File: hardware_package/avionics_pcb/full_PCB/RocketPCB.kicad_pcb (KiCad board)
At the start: 2 copper layers, 74 parts, among them J1 USB_C_Receptacle, J2 Micro_SD_Card, J3 Conn_01x03_Female, Q1 DMG2301L, Q2 Q_PMOS_DGS, SW1 SW_Push, SW2 SW_Push, U1 STM32F405RGTx, U2 TPS62160DSG, U3 Radio_Header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

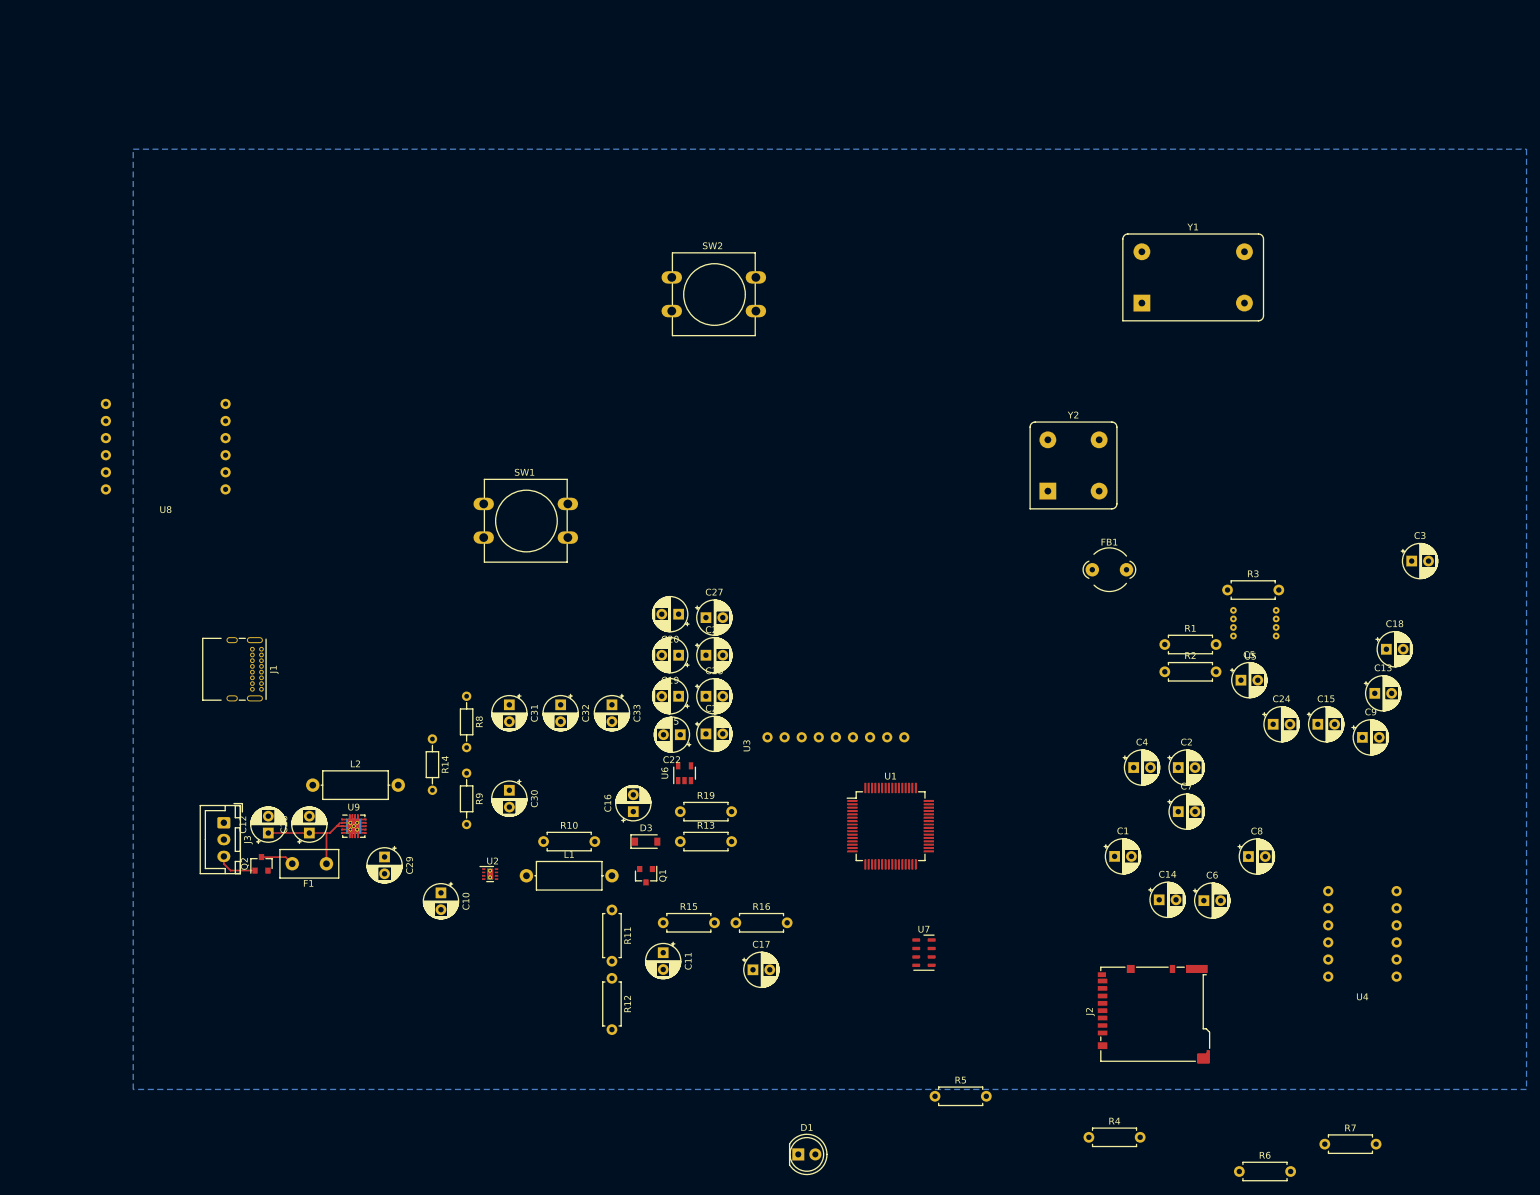
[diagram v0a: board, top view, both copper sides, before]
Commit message: Added test points and LEDs for debug, also added decoupling capacitors
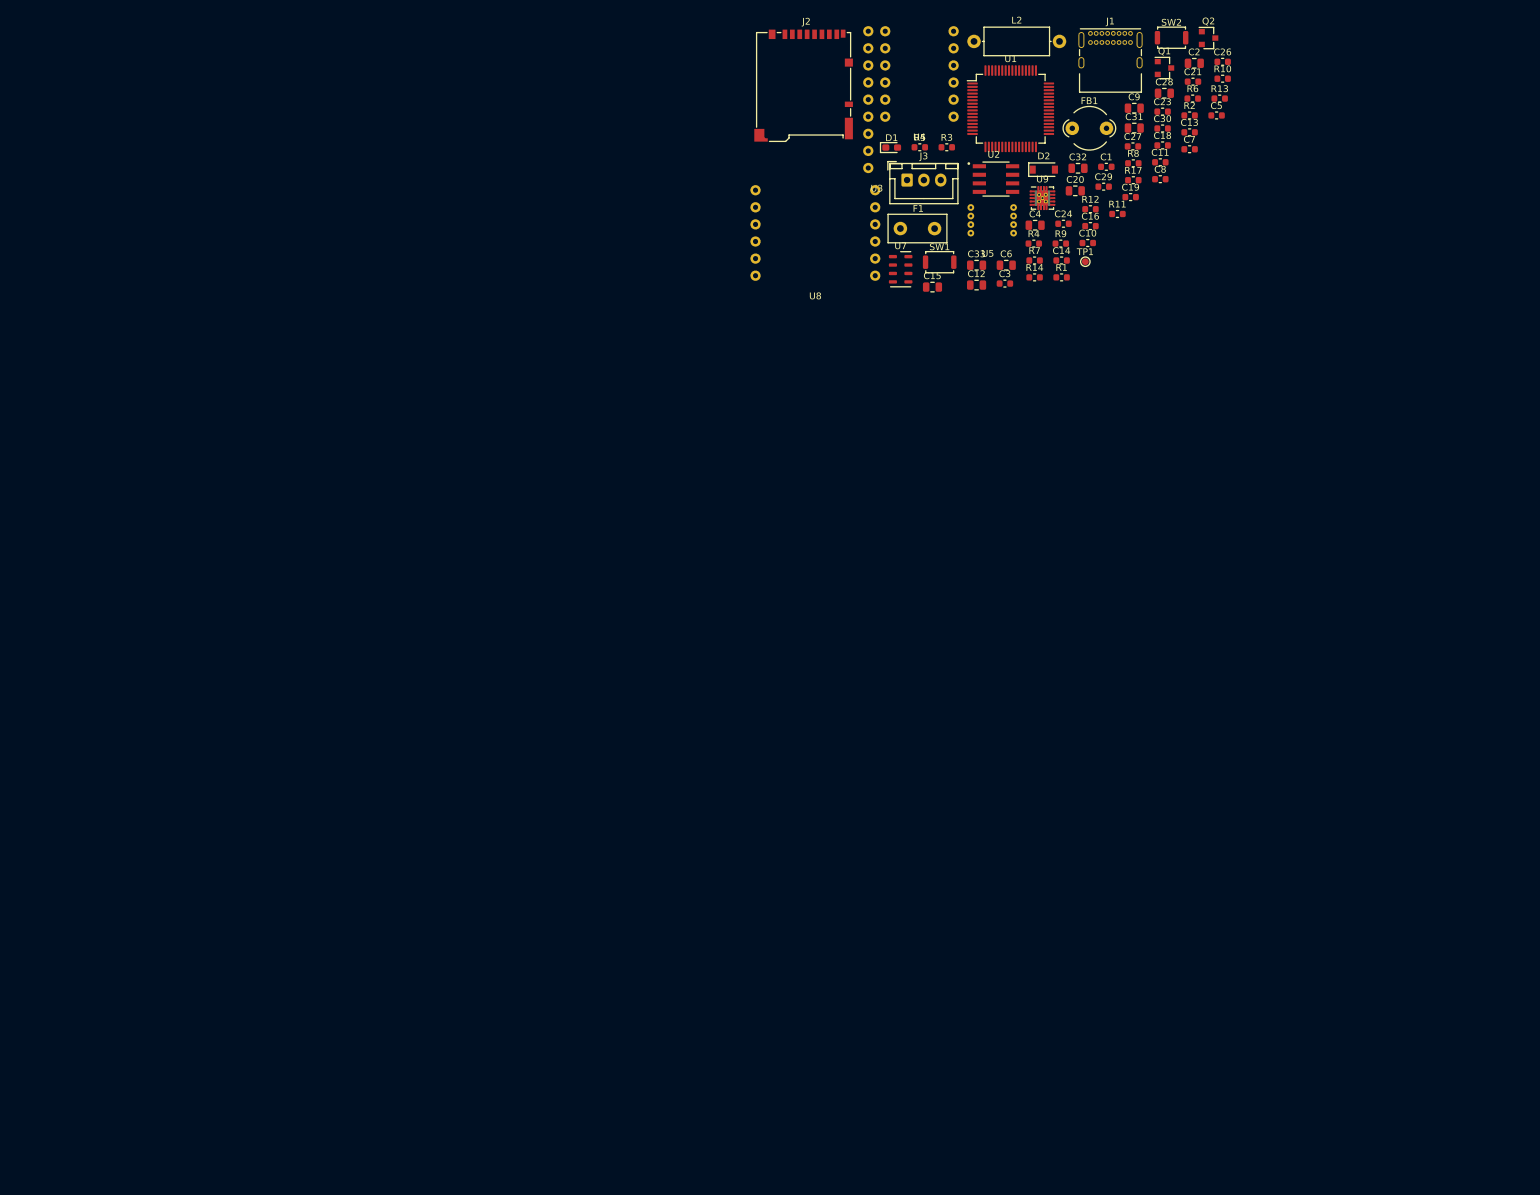
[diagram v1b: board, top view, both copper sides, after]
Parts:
- removed C17, C25: 1uF, Capacitor_THT:CP_Radial_D5.0mm_P2.50mm
- removed C22: 10uF, Capacitor_THT:CP_Radial_D5.0mm_P2.50mm
- removed D3: MBR0540, Diode_SMD:D_SOD-123
- removed L1: 2.2uH, Inductor_THT:L_Axial_L9.5mm_D4.0mm_P12.70mm_Horizontal_Fastron_SMCC
- removed R15, R16: 100k, Resistor_THT:R_Axial_DIN0207_L6.3mm_D2.5mm_P7.62mm_Horizontal
- removed R19: 10k, Resistor_THT:R_Axial_DIN0207_L6.3mm_D2.5mm_P7.62mm_Horizontal
- removed U6: AP2112K-3.3, Package_TO_SOT_SMD:SOT-23-5
- removed Y1: 12MHz, Oscillator:Oscillator_DIP-14_LargePads
- removed Y2: 32MHz, Oscillator:Oscillator_DIP-8_LargePads
- added D2: MBR0540, Diode_SMD:D_SOD-123, F.Cu at (215.3, 13.2)
- added R17: 4.7k, Resistor_SMD:R_0603_1608Metric, F.Cu at (228.6, 14.8)
- added TP1: TestPoint, TestPoint:TestPoint_Pad_D1.0mm, F.Cu at (221.5, 26.9)
- C1, C3: value 22pF -> 1uF; footprint Capacitor_THT:CP_Radial_D5.0mm_P2.50mm -> Capacitor_SMD:C_0603_1608Metric
- C10, C16: value 10uF -> 0.1uF; footprint Capacitor_THT:CP_Radial_D5.0mm_P2.50mm -> Capacitor_SMD:C_0603_1608Metric
- C11: value 22uF -> 0.1uF; footprint Capacitor_THT:CP_Radial_D5.0mm_P2.50mm -> Capacitor_SMD:C_0603_1608Metric
- C12, C15, C20, C28, C31, C32, C33, C4, C6, C9: footprint Capacitor_THT:CP_Radial_D5.0mm_P2.50mm -> Capacitor_SMD:C_0805_2012Metric
- C13: value 0.1u -> 0.1uF; footprint Capacitor_THT:CP_Radial_D5.0mm_P2.50mm -> Capacitor_SMD:C_0603_1608Metric
- C14: value 2.2u -> 2.2uF; footprint Capacitor_THT:CP_Radial_D5.0mm_P2.50mm -> Capacitor_SMD:C_0603_1608Metric
- C18, C19, C21, C23, C24, C26, C27, C29, C30, C5, C8: footprint Capacitor_THT:CP_Radial_D5.0mm_P2.50mm -> Capacitor_SMD:C_0603_1608Metric
- C2: value 22pF -> 10uF; footprint Capacitor_THT:CP_Radial_D5.0mm_P2.50mm -> Capacitor_SMD:C_0805_2012Metric
- C7: value 22pF -> C; footprint Capacitor_THT:CP_Radial_D5.0mm_P2.50mm -> Capacitor_SMD:C_0603_1608Metric
- D1: footprint LED_THT:LED_D5.0mm_Clear -> LED_SMD:LED_0603_1608Metric_Pad1.05x0.95mm_HandSolder
- Q2: value Q_PMOS_DGS -> DMG2301L
- R1, R2, R3, R4, R5, R6, R7: footprint Resistor_THT:R_Axial_DIN0207_L6.3mm_D2.5mm_P7.62mm_Horizontal -> Resistor_SMD:R_0603_1608Metric
- R10: value 100k -> 10k; footprint Resistor_THT:R_Axial_DIN0207_L6.3mm_D2.5mm_P7.62mm_Horizontal -> Resistor_SMD:R_0603_1608Metric
- R11: value 649k -> 100k; footprint Resistor_THT:R_Axial_DIN0207_L6.3mm_D2.5mm_P7.62mm_Horizontal -> Resistor_SMD:R_0603_1608Metric
- R12: value 180k -> 4.7K; footprint Resistor_THT:R_Axial_DIN0207_L6.3mm_D2.5mm_P7.62mm_Horizontal -> Resistor_SMD:R_0603_1608Metric
- R13: value 100k -> 4.7k; footprint Resistor_THT:R_Axial_DIN0207_L6.3mm_D2.5mm_P7.62mm_Horizontal -> Resistor_SMD:R_0603_1608Metric
- R14, R8, R9: footprint Resistor_THT:R_Axial_DIN0204_L3.6mm_D1.6mm_P7.62mm_Horizontal -> Resistor_SMD:R_0603_1608Metric
- SW1, SW2: footprint Button_Switch_THT:SW_PUSH-12mm -> Button_Switch_SMD:SW_Push_SPST_NO_Alps_SKRK
- U2: value TPS62160DSG -> UCC381DP-3; footprint Package_SON:WSON-8-1EP_2x2mm_P0.5mm_EP0.9x1.6mm_ThermalVias -> 3v3 _linReg:SOIC127P599X175-8N
- moved Q2 186.7 mm to (239.8, -6.35), turned to 0 degrees
- moved C28 168.0 mm to (233.2, 1.85), turned to 0 degrees
- moved R6 159.6 mm to (237.4, 2.64)
- moved J1 153.4 mm to (222.2, -7.04), turned to 0 degrees
- moved R10 151.7 mm to (241.9, -0.31)
- moved D1 150.2 mm to (192.7, 9.92)
- moved L2 147.9 mm to (204.9, -5.85)
- moved J2 147.5 mm to (179.6, 0.72), turned to 0 degrees
- moved C29 146.1 mm to (224.2, 15.7), turned to 0 degrees
- moved U4 143.7 mm to (196.8, 7.87)
- moved Q1 142.6 mm to (233.2, -1.90), turned to 0 degrees
- moved R5 141.0 mm to (196.9, 9.88)
- moved J3 139.4 mm to (195.0, 14.7), turned to 0 degrees
- moved C11 138.7 mm to (232.6, 12.1), turned to 0 degrees
- moved U9 138.5 mm to (215.1, 17.4)
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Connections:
- net /~RESET~ renamed ~RESET~
- C1 pad 1: Net-(C1-Pad1) -> +3V3
- C10 pad 1: +7.5V -> GND
- C10 pad 2: GND -> +3V3
- C11 pad 1: +BATT -> +3V3
- C12 pad 1: +7.5V -> +7V4
- C16 pad 1: Net-(C16-Pad1) -> +3V3
- C2 pad 1: Net-(C2-Pad1) -> GND
- C2 pad 2: GND -> +3V3
- C28 pad 1: +7.5V -> +7V4
- C7 pad 1: Net-(C3-Pad1) -> +3V3
- C8 pad 1: VCC -> Net-(C8-Pad1)
- C9 pad 1: VCC -> Net-(C8-Pad1)
- F1 pad 1: +7.5V -> +7V4
- FB1 pad 2: VCC -> Net-(C8-Pad1)
- Q1 pad 1: VBUS -> +7V4
- Q1 pad 2: Net-(C16-Pad1) -> VBUS
- Q1 pad 3: +BATT -> Net-(C3-Pad1)
- Q2 pad 1: Net-(J3-Pad3) -> GND
- Q2 pad 2: GND -> Net-(F1-Pad2)
- Q2 pad 3: Net-(F1-Pad2) -> Net-(J3-Pad3)
- R10 pad 1: /PG -> Net-(C3-Pad1)
- R10 pad 2: +BATT -> Net-(R10-Pad2)
- R11 pad 1: +BATT -> +7V4
- R11 pad 2: Net-(R11-Pad2) -> GND
- R12 pad 1: Net-(R11-Pad2) -> +3V3
- R12 pad 2: GND -> /FLASH_CS
- R13 pad 1: VBUS -> /SCL
- R13 pad 2: GND -> +3V3
- U1 pad 1: +BATT -> Net-(TP1-Pad1)
- U1 pad 13: VCC -> Net-(C8-Pad1)
- U1 pad 14: /RXI -> /PWM0
- U1 pad 15: /TX0 -> /PWM1
- U1 pad 17: /V_DIV -> Net-(U1-Pad17)
- U1 pad 19: +3V3 -> Net-(C8-Pad1)
- U1 pad 3: Net-(C3-Pad1) -> Net-(U1-Pad3)
- U1 pad 32: +3V3 -> Net-(C8-Pad1)
- U1 pad 48: +3V3 -> Net-(C8-Pad1)
- U1 pad 5: Net-(C1-Pad1) -> Net-(U1-Pad5)
- U1 pad 50: +3V3 -> Net-(U1-Pad50)
- U1 pad 6: Net-(C2-Pad1) -> Net-(U1-Pad6)
- U1 pad 64: +3V3 -> Net-(C8-Pad1)
- U2 pad 1: GND -> +3V3
- U2 pad 2: +7.5V -> GND
- U2 pad 3: +7.5V -> GND
- U2 pad 4: GND -> +3V3
- U2 pad 5: Net-(R11-Pad2) -> Net-(R10-Pad2)
- U2 pad 6: +BATT -> GND
- U2 pad 7: Net-(L1-Pad1) -> GND
- U2 pad 8: /PG -> Net-(C3-Pad1)
- U3 pad 3: Net-(U3-Pad3) -> +3V3
- U5 pad 1: +3V3 -> /FLASH_CS
- U8 pad 8: /TX0 -> /TX_D1
- U8 pad 9: /RXI -> /RX_D0
- U9 pad 2: +7.5V -> +7V4
- U9 pad 3: +7.5V -> +7V4
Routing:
- net +7.5V: track 16.9 -> 0.00 mm
- net Net-(J3-Pad3): track 6.15 -> 0.00 mm
- net Net-(F1-Pad2): track 4.98 -> 0.00 mm
- removed copper zone on B.Cu, net GND
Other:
- rule pad_to_mask_clearance: 0.05 -> 0
- rule trace_min: 0.25 -> 0.2

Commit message: Fixed IMU, USB & JR conn fp/p/o conflict, laid out PCB blocks
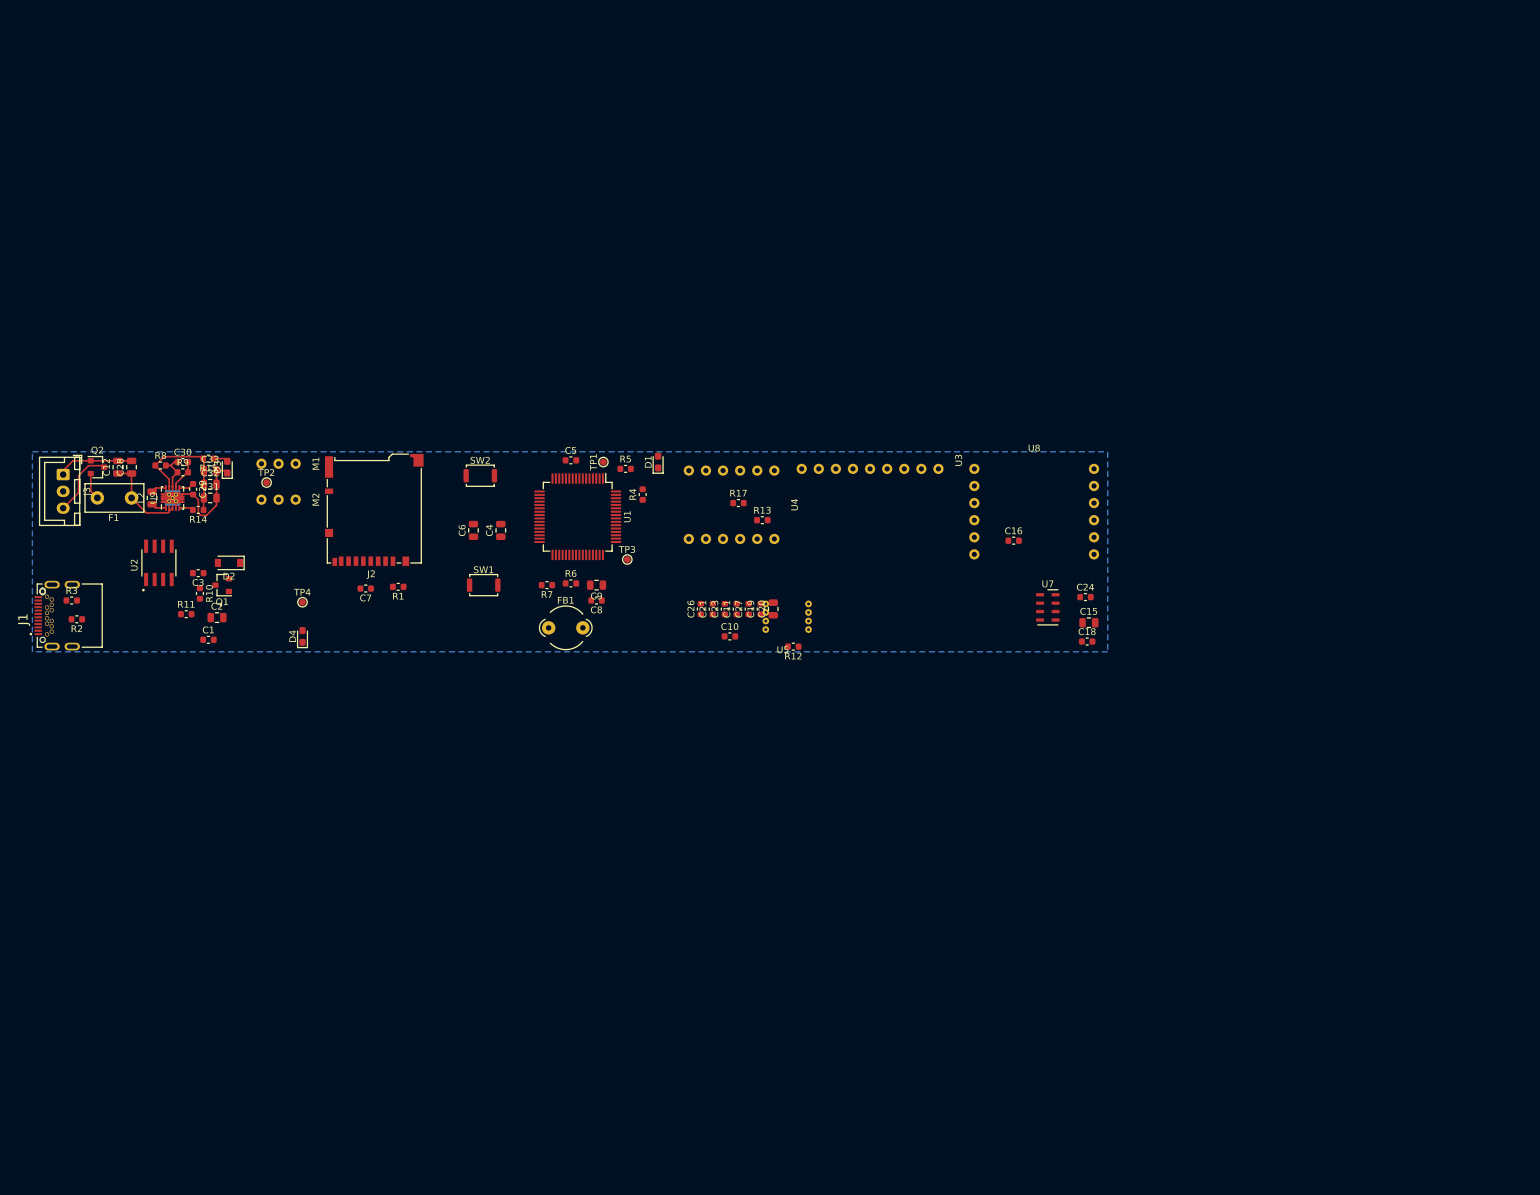
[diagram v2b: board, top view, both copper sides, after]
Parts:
- removed C13: 0.1uF, Capacitor_SMD:C_0603_1608Metric
- removed C14: 2.2uF, Capacitor_SMD:C_0603_1608Metric
- added D3: LED, LED_SMD:LED_0603_1608Metric_Pad1.05x0.95mm_HandSolder, F.Cu at (94.0, 57.4)
- added D4: LED, LED_SMD:LED_0603_1608Metric_Pad1.05x0.95mm_HandSolder, F.Cu at (105.2, 82.5)
- added M1: Motor_Servo_JR, GPS_head0:JR_servo_connector, F.Cu at (106.7, 56.9)
- added M2: Motor_Servo_JR, GPS_head0:JR_servo_connector, F.Cu at (106.7, 62.2)
- added R15: 46, Resistor_SMD:R_0603_1608Metric, F.Cu at (91.2, 56.1)
- added TP2: TestPoint, TestPoint:TestPoint_Pad_D1.0mm, F.Cu at (99.8, 59.7)
- added TP3: TestPoint, TestPoint:TestPoint_Pad_D1.0mm, F.Cu at (153.4, 71.1)
- added TP4: TestPoint, TestPoint:TestPoint_Pad_D1.0mm, F.Cu at (105.2, 77.5)
- J1: value USB_C_Receptacle -> DX07S024XJ1R1100; footprint Connector_USB:USB_C_Receptacle_GCT_USB4085 -> DX07S024XJ1R1100:JAE_DX07S024XJ1R1100
- L2: footprint Inductor_THT:L_Axial_L9.5mm_D4.0mm_P12.70mm_Horizontal_Fastron_SMCC -> Inductor_SMD:L_0805_2012Metric
- U4: value MPU-6050 -> MPU6050_BO_FP
- moved R2 181.5 mm to (71.6, 80.0), turned to 180 degrees
- moved J1 179.9 mm to (66.5, 83.1), turned to 90 degrees
- moved Q2 177.0 mm to (74.7, 57.4)
- moved R10 170.1 mm to (89.9, 76.2), turned to 270 degrees
- moved C2 166.9 mm to (92.5, 79.8)
- moved C28 163.2 mm to (79.8, 57.4), turned to 90 degrees
- moved Q1 159.7 mm to (93.2, 74.9), turned to 180 degrees
- moved C30 153.8 mm to (87.4, 56.6)
- moved R8 151.3 mm to (84.1, 57.1)
- moved C1 150.8 mm to (91.2, 83.1)
- moved R11 150.6 mm to (87.9, 79.2)
- moved C31 147.9 mm to (91.4, 62.0)
- moved R3 146.4 mm to (70.9, 77.2)
- moved C29 142.6 mm to (88.9, 60.7), turned to 270 degrees
- moved L2 139.7 mm to (82.8, 62.0), turned to 90 degrees
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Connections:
- R2 pad 2: Net-(J1-PadB5) -> Net-(J1-PadA5)
- R3 pad 2: Net-(J1-PadA5) -> Net-(J1-PadB5)
- U4 pad 1: GND -> +3V3
- U4 pad 12: /INT -> Net-(U4-Pad12)
- U4 pad 2: (no net) -> Net-(U4-Pad2)
- U4 pad 3: (no net) -> GND
- U4 pad 4: (no net) -> /SCL
- U4 pad 5: (no net) -> /SDA
- U4 pad 6: Net-(U4-Pad6) -> /INT
- U4 pad 7: Net-(U4-Pad7) -> GND
- U4 pad 8: +3V3 -> /CLKIN
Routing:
- net GND: track 0.00 -> 37.6 mm
- net +6V: track 0.00 -> 19.7 mm
- net +7V4: track 0.00 -> 13.6 mm
- net Net-(J3-Pad3): track 0.00 -> 10.3 mm
- net Net-(C30-Pad1): track 0.00 -> 6.00 mm
- net Net-(F1-Pad2): track 0.00 -> 4.02 mm
- net Net-(C29-Pad1): track 0.00 -> 2.30 mm
- net Net-(L2-Pad2): track 0.00 -> 2.27 mm
- net Net-(L2-Pad1): track 0.00 -> 2.27 mm
- net Net-(D3-Pad2): track 0.00 -> 2.17 mm
- net Net-(R14-Pad2): track 0.00 -> 2.15 mm
- added copper zone on B.Cu, net GND
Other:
- board outline added: 0.8 x 1 mm
